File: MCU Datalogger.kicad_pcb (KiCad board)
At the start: 2 copper layers, 0 parts

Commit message: Setup PCB-new
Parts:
- added BT1: Battery, Connector_PinHeader_2.54mm:PinHeader_1x02_P2.54mm_Vertical, F.Cu at (112.8, 91.8)
- added C1: 0.1uF, Capacitor_SMD:C_0805_2012Metric, F.Cu at (135.1, 81.9)
- added C2: 22pF, Capacitor_SMD:C_0805_2012Metric, F.Cu at (135.1, 84.9)
- added C3: 22pF, Capacitor_SMD:C_0805_2012Metric, F.Cu at (135.1, 87.9)
- added C4: 0.1uF, Capacitor_SMD:C_0805_2012Metric, F.Cu at (135.1, 90.9)
- added C5: 100nF, Capacitor_SMD:C_0805_2012Metric, F.Cu at (135.1, 94.0)
- added D1: LED, LED_SMD:LED_0805_2012Metric, F.Cu at (139.6, 81.9)
- added D2: LED, LED_SMD:LED_0805_2012Metric, F.Cu at (139.6, 85.0)
- added H1: MountingHole, MountingHole:MountingHole_2.1mm, F.Cu at (113.4, 69.4)
- added H2: MountingHole, MountingHole:MountingHole_2.1mm, F.Cu at (113.4, 75.1)
- added H3: MountingHole, MountingHole:MountingHole_2.1mm, F.Cu at (113.4, 80.9)
- added H4: MountingHole, MountingHole:MountingHole_2.1mm, F.Cu at (113.4, 86.6)
- added J1: Conn_01x04_Pin, Connector_PinHeader_2.54mm:PinHeader_1x04_P2.54mm_Vertical, F.Cu at (150.7, 68.8)
- added J2: Conn_01x09_Pin, Connector_PinHeader_2.54mm:PinHeader_1x09_P2.54mm_Vertical, F.Cu at (146.1, 68.8)
- added J3: Conn_01x04_Pin, Connector_PinHeader_2.54mm:PinHeader_1x04_P2.54mm_Vertical, F.Cu at (155.3, 68.8)
- added J4: Conn_02x03_Odd_Even, Connector_PinHeader_2.54mm:PinHeader_2x03_P2.54mm_Vertical, F.Cu at (150.7, 81.0)
- added R1: 10K, Resistor_SMD:R_0805_2012Metric, F.Cu at (118.5, 68.0)
- added R2: 10K, Resistor_SMD:R_0805_2012Metric, F.Cu at (118.5, 70.9)
- added R3: 4.7K, Resistor_SMD:R_0805_2012Metric, F.Cu at (118.5, 73.9)
- added R4: 4.7K, Resistor_SMD:R_0805_2012Metric, F.Cu at (118.5, 76.8)
- added R5: 330, Resistor_SMD:R_0805_2012Metric, F.Cu at (118.5, 79.8)
- added R6: 10K, Resistor_SMD:R_0805_2012Metric, F.Cu at (118.5, 82.7)
- added R7: 330, Resistor_SMD:R_0805_2012Metric, F.Cu at (118.5, 85.7)
- added U1: 24LC1025, Package_SO:SOIC-8_5.3x5.3mm_P1.27mm, F.Cu at (125.8, 70.0)
- added U2: DS1337S_, DS1337S_:SOIC127P600X175-8N, F.Cu at (125.8, 95.0)
- added U3: 24LC1025, Package_SO:SOIC-8_5.3x5.3mm_P1.27mm, F.Cu at (125.8, 77.0)
- added U4: ATMEGA328P-AU, ATMEGA328P-AU:QFP80P900X900X120-32N, F.Cu at (127.2, 86.1)
- added Y1: 32.768 kHZ, Crystal:Crystal_SMD_5032-2Pin_5.0x3.2mm_HandSoldering, F.Cu at (136.2, 69.1)
- added Y2: 16 MHz, Crystal:Crystal_SMD_5032-2Pin_5.0x3.2mm_HandSoldering, F.Cu at (136.2, 74.4)

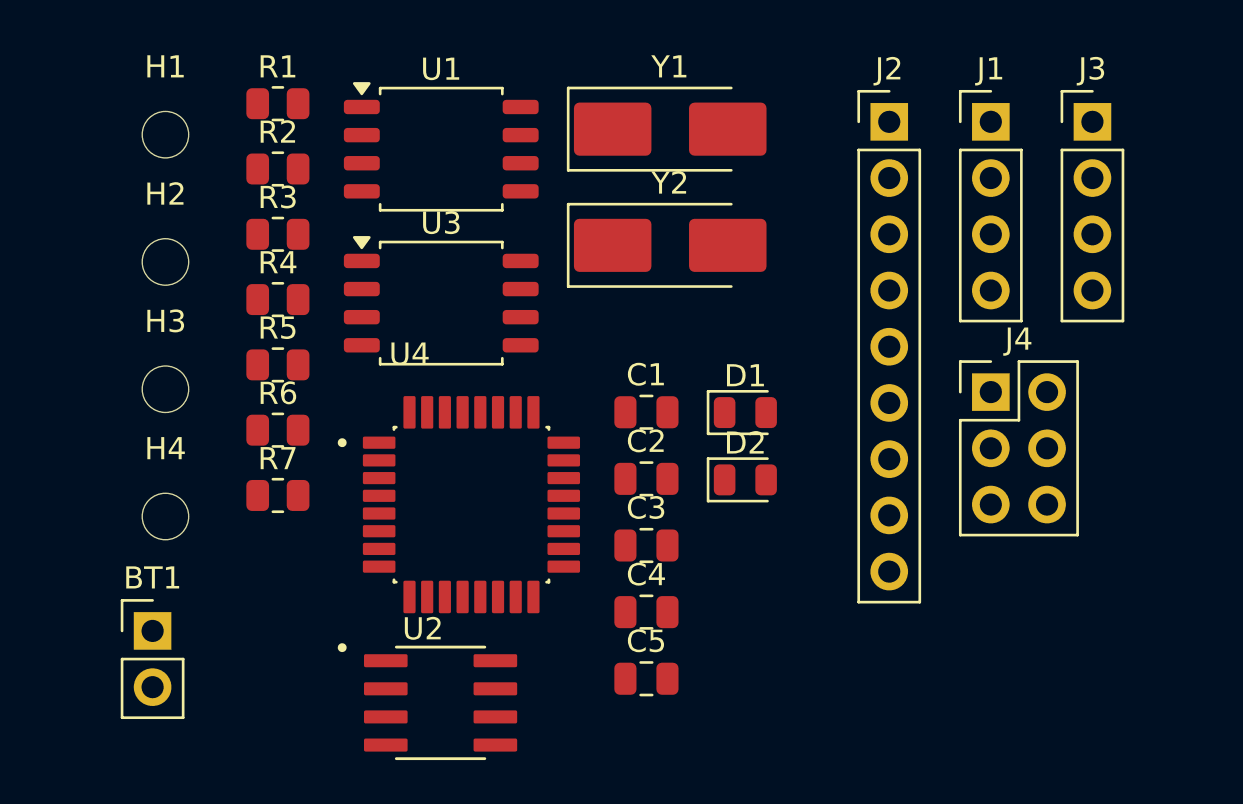
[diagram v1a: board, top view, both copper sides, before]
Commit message: Completed placement of footprints
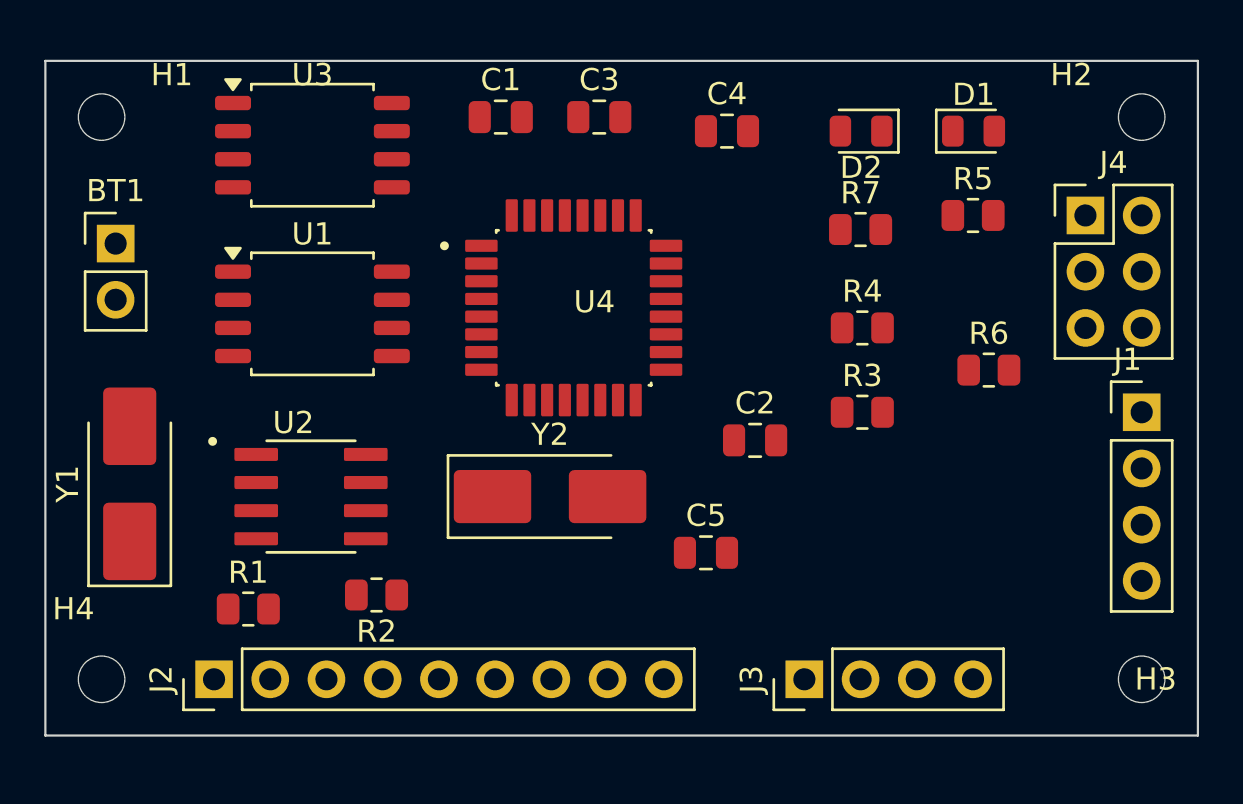
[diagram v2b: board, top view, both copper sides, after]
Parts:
- moved H3 46.0 mm to (157.5, 94.0)
- moved H2 44.6 mm to (157.5, 68.6)
- moved J2 39.6 mm to (115.6, 94.0), turned to 90 degrees
- moved R6 32.2 mm to (150.6, 80.0)
- moved R5 32.1 mm to (149.9, 73.0)
- moved Y1 29.2 mm to (111.8, 85.2), turned to 90 degrees
- moved R7 28.9 mm to (144.8, 73.7)
- moved J3 28.3 mm to (142.2, 94.0), turned to 90 degrees
- moved R3 27.6 mm to (144.9, 81.9)
- moved R4 26.4 mm to (144.9, 78.1)
- moved R1 22.9 mm to (117.1, 90.8)
- moved C4 22.0 mm to (138.7, 69.2)
- moved R2 19.8 mm to (122.9, 90.2), turned to 180 degrees
- moved C3 19.5 mm to (133.0, 68.6)
- moved BT1 17.6 mm to (111.1, 74.3)
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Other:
- board outline added: 52.1 x 30.5 mm

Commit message: Routing VCC GND Complete
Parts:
- moved C4 21.3 mm to (145.1, 89.5), turned to 180 degrees
- moved C5 19.7 mm to (138.1, 68.6), turned to 180 degrees
- moved C2 5.99 mm to (145.1, 86.4), turned to 180 degrees
- moved U1 0.64 mm to (120.0, 76.8)
- turned D2 to 0 degrees
- turned R3 to 180 degrees
- turned R4 to 180 degrees
- turned R6 to 180 degrees
- turned Y2 to 180 degrees
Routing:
- net /VCC: track 0.00 -> 167.8 mm, vias 0 -> 6
- net /SCK: track 0.00 -> 111.5 mm, vias 0 -> 8
- net /SDA: track 0.00 -> 72.0 mm, vias 0 -> 2
- net Net-(BT1-+): track 0.00 -> 71.2 mm, vias 0 -> 5
- net GND: track 0.00 -> 60.2 mm, vias 0 -> 4
- net /TX: track 0.00 -> 39.9 mm, vias 0 -> 1
- net /RX: track 0.00 -> 39.2 mm, vias 0 -> 1
- net Net-(U4-PB7): track 0.00 -> 35.8 mm, vias 0 -> 4
- net /MOSI: track 0.00 -> 33.9 mm
- net /RESET: track 0.00 -> 31.2 mm, vias 0 -> 4
- net Net-(U4-PB6): track 0.00 -> 28.0 mm
- net /D8: track 0.00 -> 27.1 mm, vias 0 -> 1
- net /D2: track 0.00 -> 26.6 mm, vias 0 -> 1
- net /D7: track 0.00 -> 26.3 mm, vias 0 -> 1
- net /D3: track 0.00 -> 26.3 mm
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
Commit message: Completed Routing
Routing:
- net GND: track 60.2 -> 112.2 mm, vias 4 -> 10
- net /VCC: track 167.8 -> 174.6 mm, vias 6 -> 8
- net /D3: track 26.3 -> 30.3 mm, vias 0 -> 2
- net /D7: track 26.3 -> 25.3 mm
- net Net-(BT1-+): track 71.2 -> 71.8 mm
- added copper zone on F.Cu, net /VCC
- added copper zone on B.Cu, net GND

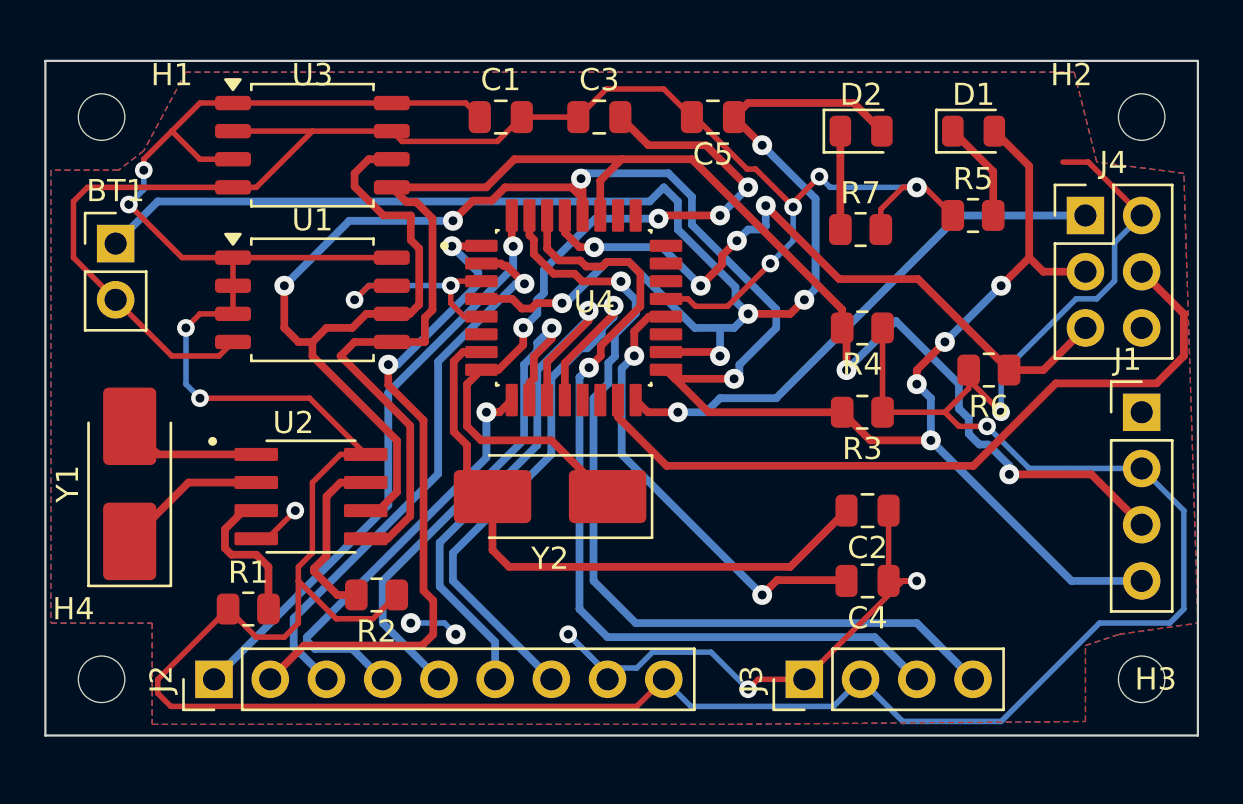
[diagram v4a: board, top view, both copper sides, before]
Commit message: Complete PCB Layout and DRC Check Complete
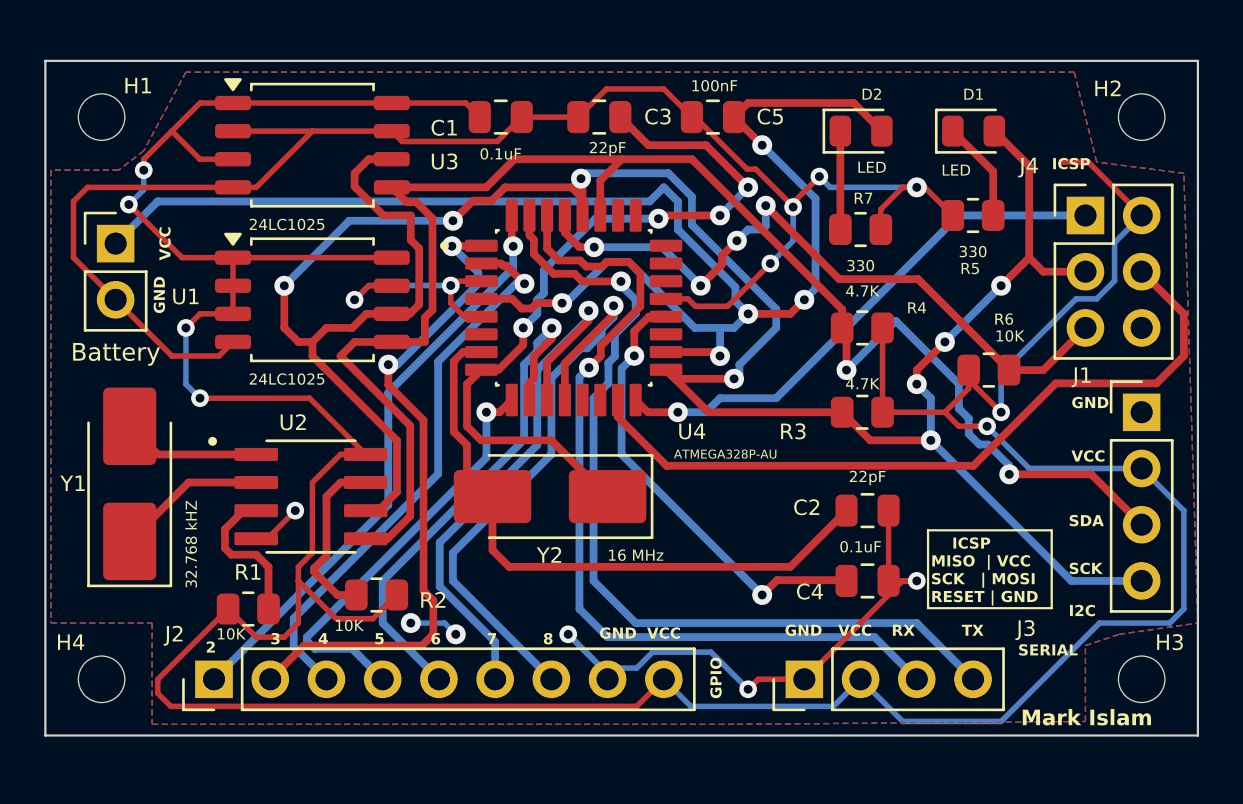
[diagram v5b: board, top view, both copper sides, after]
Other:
- board text added: "2"
- board text added: "3"
- board text added: "4"
- board text added: "5"
- board text added: "6"
- board text added: "7"
- board text added: "8"
- board text added: "GND"
- board text added: "GPIO"
- board text added: "I2C"
- board text added: "ICSP"
- board text added: "ICSP MISO | VCC SCK | MOSI RESET | GND"
- board text added: "Mark Islam"
- board text added: "RX"
- board text added: "SCK"
- board text added: "SDA"
- board text added: "SERIAL"
- board text added: "TX"
- board text added: "VCC"
